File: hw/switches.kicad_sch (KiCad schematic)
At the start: 46 parts, among them SW1 SW_Push, SW10 SW_Push, SW11 SW_Push, SW12 SW_Push, SW13 SW_Push, SW14 SW_Push, SW15 SW_Push, SW16 SW_Push, SW17 SW_Push, SW18 SW_Push, SW19 SW_Push, SW2 SW_Push, SW20 SW_Push, SW21 SW_Push, SW3 SW_Push, SW4 SW_Push, SW5 SW_Push, SW6 SW_Push, SW7 SW_Push, SW8 SW_Push, SW9 SW_Push

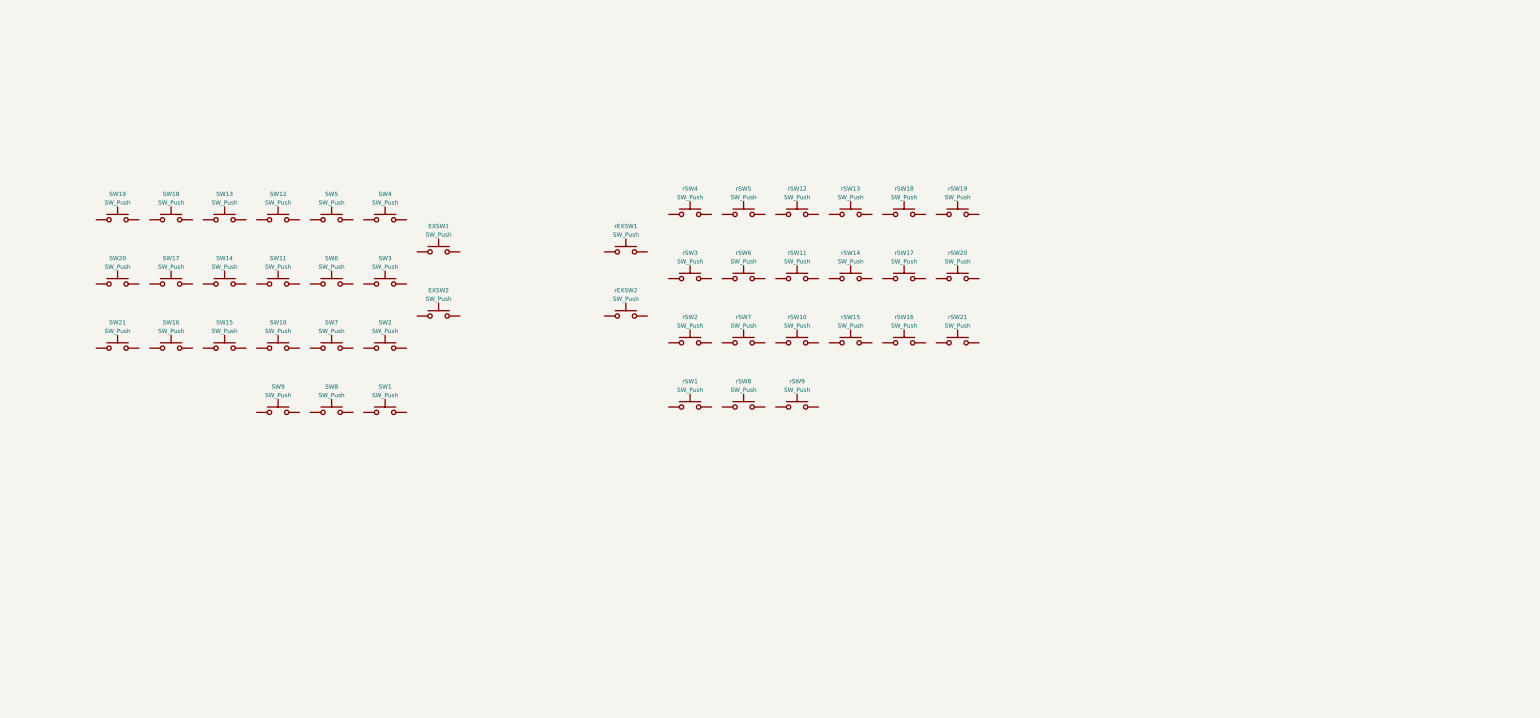
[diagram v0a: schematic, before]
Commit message: Power schematic with npm1100 setup
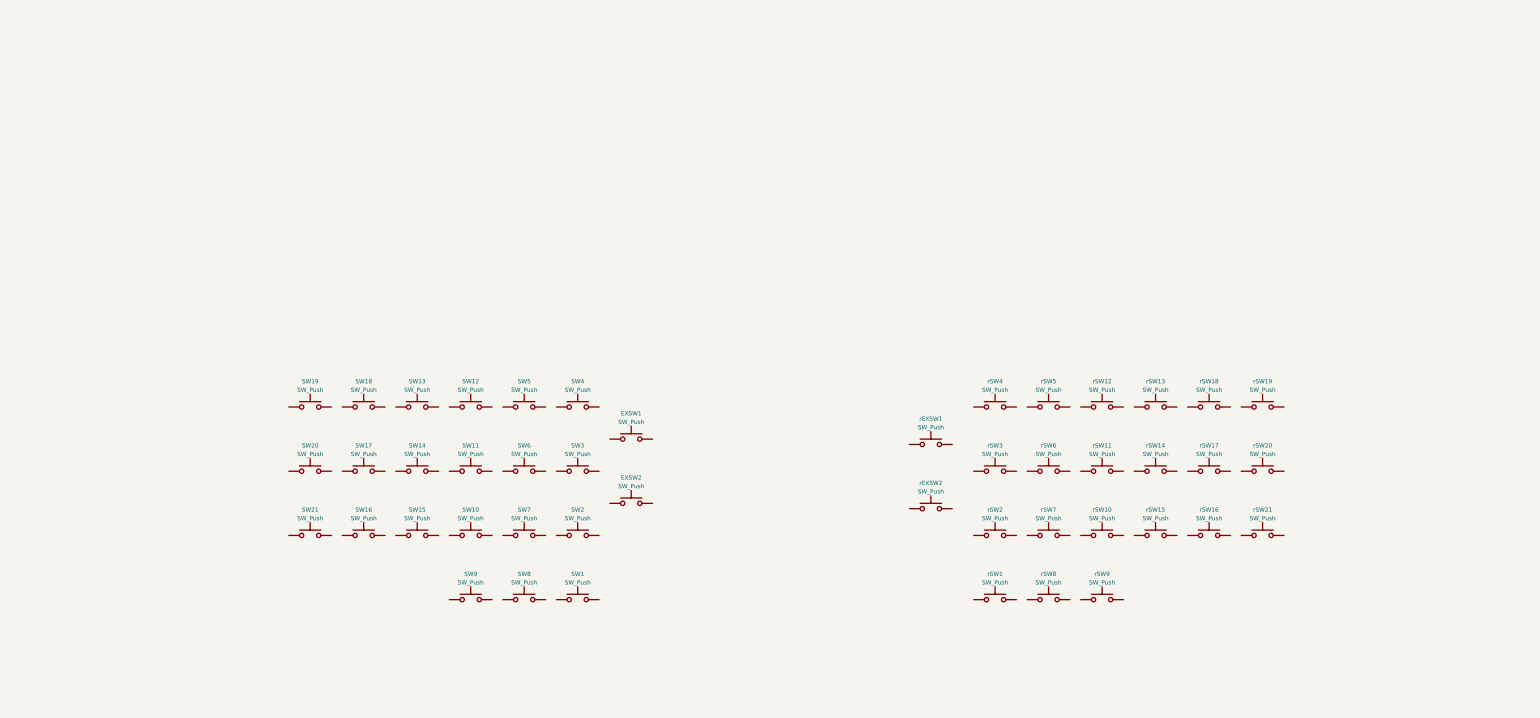
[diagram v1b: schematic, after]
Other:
- moved on the sheet: EXSW1, EXSW2, SW1, SW10, SW11, SW12, SW13, SW14, SW15, SW16, SW17, SW18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

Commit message: Switch matrix and sheet pins
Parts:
- added D1, D10, D11, D12, D13, D14, D15, D16, D17, D18, D19, D2, D20, D21, D22, D23, D3, D4, D5, D6, D7, D8, D9, rD1, rD10, rD11, rD12, rD13, rD14, rD15, rD16, rD17, rD18, rD19, rD2, rD20, rD21, rD22, rD23, rD3, rD4, rD5, rD6, rD7, rD8, rD9: D, symbol Alidade:D
- renumbered EXSW1 to SW22, EXSW2 to SW23, rEXSW1 to rSW22, rEXSW2 to rSW23
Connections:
- net at rSW6.1: now also rD6.2 (A)
- net rCOL2: now reaches rSW6.2
- net rCOL2: now also rSW5.2, rSW7.2, rSW8.2
- net at rSW4.1: now also rD4.2 (A)
- net rCOL1: now reaches rSW4.2
- net rCOL1: now also rSW1.2, rSW2.2, rSW3.2
- net at SW5.1: now also D5.2 (A)
- net COL2: now reaches SW5.2
- net COL2: now also SW6.2, SW7.2, SW8.2
- net at SW4.1: now also D4.2 (A)
- net COL1: now reaches SW4.2
- net COL1: now also SW1.2, SW2.2, SW3.2
- net at SW12.1: now also D12.2 (A)
- net COL3: now reaches SW12.2
- net COL3: now also SW10.2, SW11.2, SW9.2
- net at SW7.1: now also D7.2 (A)
- net at rSW5.1: now also rD5.2 (A)
- net at rSW16.1: now also rD16.2 (A)
- net rCOL5: now reaches rSW16.2
- net rCOL5: now also rSW17.2, rSW18.2
- net at SW21.1: now also D21.2 (A)
- net COL6: now reaches SW21.2
- net COL6: now also SW19.2, SW20.2
- net at rSW15.1: now also rD15.2 (A)
- net rCOL4: now reaches rSW15.2
- net rCOL4: now also rSW13.2, rSW14.2
- net at SW19.1: now also D19.2 (A)
- net at rSW1.1: now also rD1.2 (A)
- net at SW6.1: now also D6.2 (A)
- net at SW1.1: now also D1.2 (A)
- net at SW14.1: now also D14.2 (A)
- net COL4: now reaches SW14.2
- net COL4: now also SW13.2, SW15.2
- net at SW17.1: now also D17.2 (A)
- net COL5: now reaches SW17.2
- net COL5: now also SW16.2, SW18.2
- net at rSW17.1: now also rD17.2 (A)
- net at rSW21.1: now also rD21.2 (A)
- net rCOL6: now reaches rSW21.2
- net rCOL6: now also rSW19.2, rSW20.2
- net at SW16.1: now also D16.2 (A)
- net at SW15.1: now also D15.2 (A)
- net at SW18.1: now also D18.2 (A)
- net at rSW9.1: now also rD9.2 (A)
- net rCOL3: now reaches rSW9.2
- net rCOL3: now also rSW10.2, rSW11.2, rSW12.2
- net at SW23.1: now also D23.2 (A)
- net COL0: now reaches SW23.2
- net COL0: now also SW22.2
- net at rSW19.1: now also rD19.2 (A)
- net at rSW2.1: now also rD2.2 (A)
- net at rSW13.1: now also rD13.2 (A)
- net rCOL0: now reaches rSW23.1
- net rCOL0: now also rSW22.1
- net at rSW23.2: now also rD23.2 (A)
- net at rSW7.1: now also rD7.2 (A)
- net at SW2.1: now also D2.2 (A)
- net at rSW14.1: now also rD14.2 (A)
- net at rSW3.1: now also rD3.2 (A)
- net at SW11.1: now also D11.2 (A)
- net at rSW20.1: now also rD20.2 (A)
- net at SW20.1: now also D20.2 (A)
- net at rSW11.1: now also rD11.2 (A)
- net at SW22.1: now also D22.2 (A)
- net at SW13.1: now also D13.2 (A)
- net at rSW18.1: now also rD18.2 (A)
- net at rSW8.1: now also rD8.2 (A)
- net at SW8.1: now also D8.2 (A)
- net at rSW10.1: now also rD10.2 (A)
- net at rSW12.1: now also rD12.2 (A)
- net at SW9.1: now also D9.2 (A)
- net at rSW22.2: now also rD22.2 (A)
- net at SW3.1: now also D3.2 (A)
- net at SW10.1: now also D10.2 (A)
- new net ROW0: D1.1 (K), D8.1 (K), D9.1 (K)
- new net ROW1: D10.1 (K), D15.1 (K), D16.1 (K), D2.1 (K), D21.1 (K), D23.1 (K), D7.1 (K)
- new net ROW2: D11.1 (K), D14.1 (K), D17.1 (K), D20.1 (K), D22.1 (K), D3.1 (K), D6.1 (K)
- new net ROW3: D12.1 (K), D13.1 (K), D18.1 (K), D19.1 (K), D4.1 (K), D5.1 (K)
- new net rROW0: rD1.1 (K), rD8.1 (K), rD9.1 (K)
- new net rROW1: rD10.1 (K), rD15.1 (K), rD16.1 (K), rD2.1 (K), rD21.1 (K), rD23.1 (K), rD7.1 (K)
- new net rROW2: rD11.1 (K), rD14.1 (K), rD17.1 (K), rD20.1 (K), rD22.1 (K), rD3.1 (K), rD6.1 (K)
- new net rROW3: rD12.1 (K), rD13.1 (K), rD18.1 (K), rD19.1 (K), rD4.1 (K), rD5.1 (K)
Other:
- moved on the sheet: rSW22, rSW23

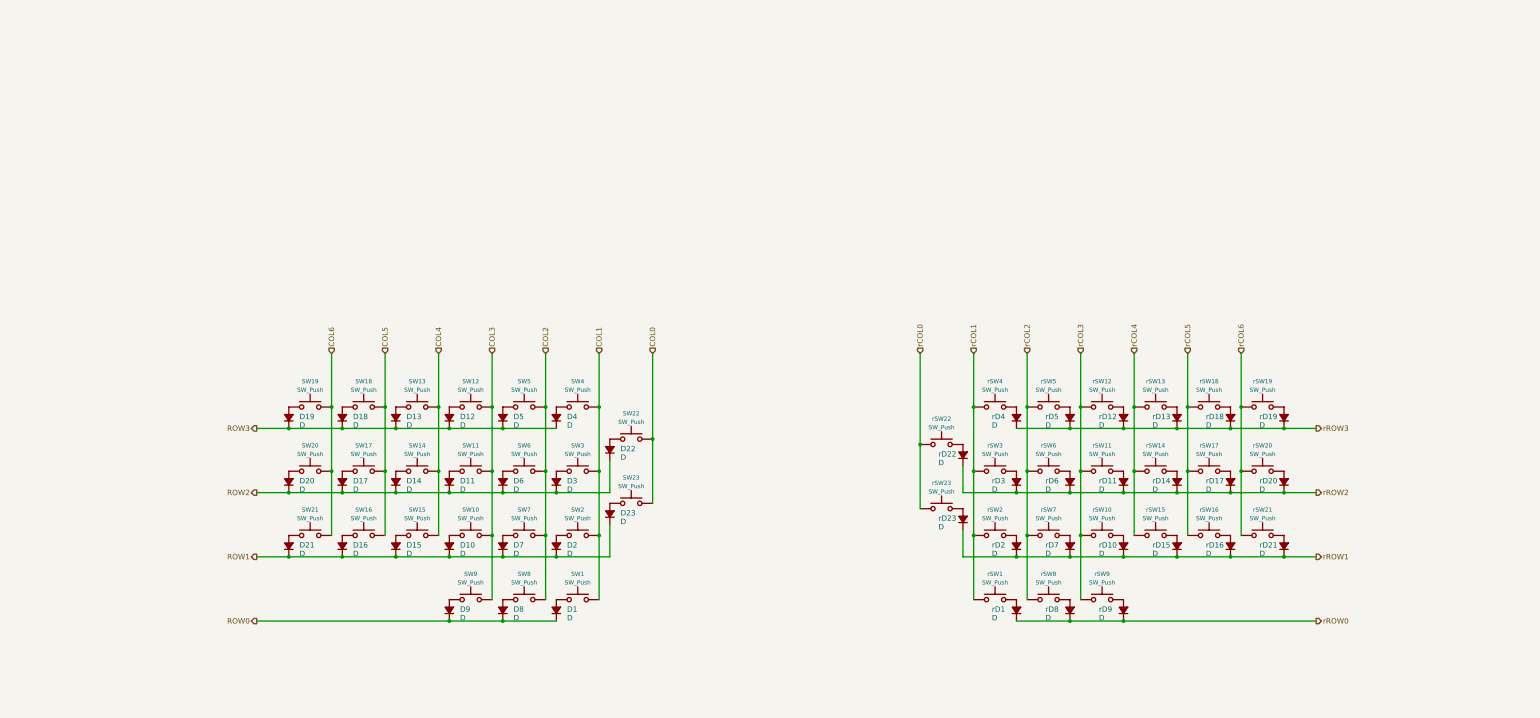
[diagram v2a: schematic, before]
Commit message: Place decoder and update switches
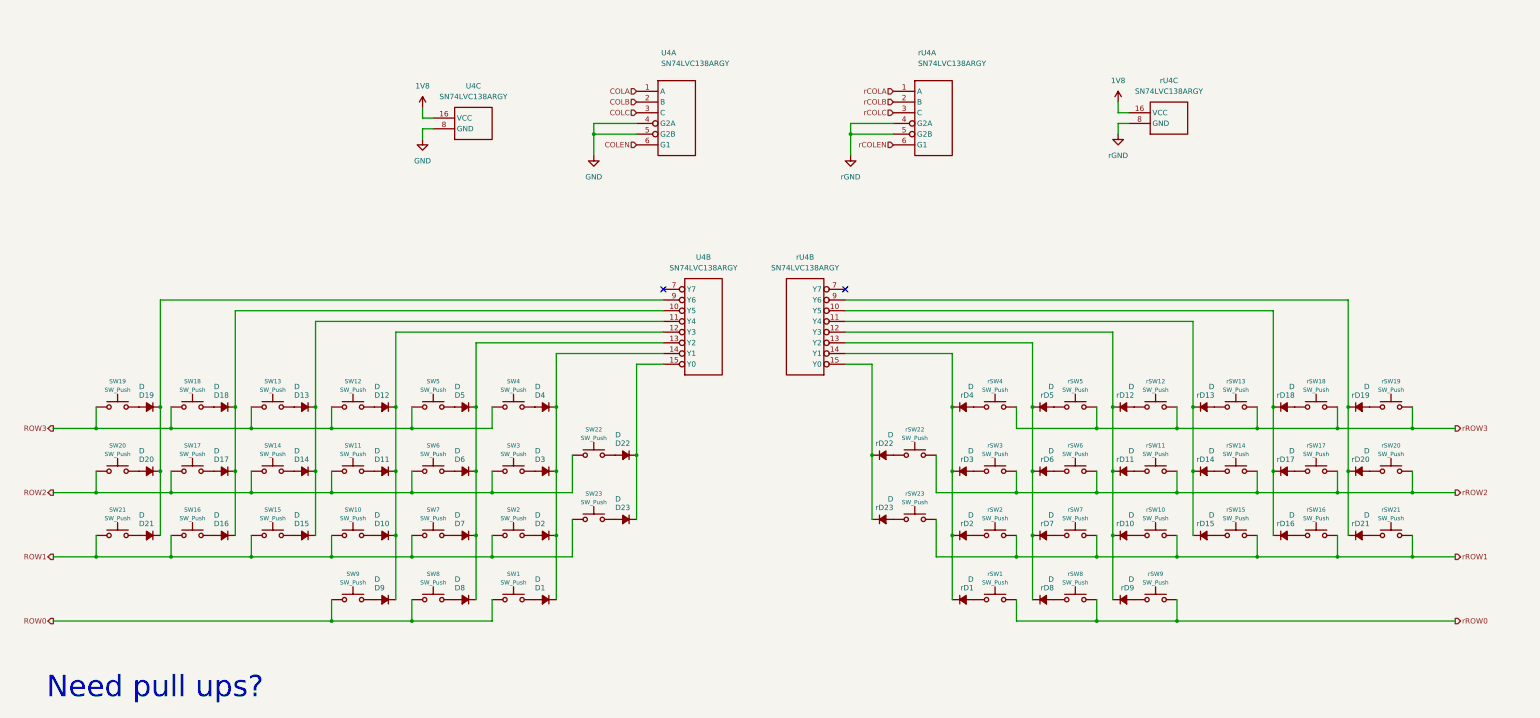
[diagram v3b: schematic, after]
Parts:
- added U4, rU4: SN74LVC138ARGY, symbol Alidade:SN74LVC138ARGY
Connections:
- net ROW0: now also SW1.1, SW8.1, SW9.1; no longer D1.1 (K), D8.1 (K), D9.1 (K)
- net ROW1: now also SW10.1, SW15.1, SW16.1, SW2.1, SW21.1, SW23.2, SW7.1; no longer D10.1 (K), D15.1 (K), D16.1 (K), D2.1 (K), D21.1 (K), D23.1 (K), D7.1 (K)
- net ROW2: now also SW11.1, SW14.1, SW17.1, SW20.1, SW22.2, SW3.1, SW6.1; no longer D11.1 (K), D14.1 (K), D17.1 (K), D20.1 (K), D22.1 (K), D3.1 (K), D6.1 (K)
- net ROW3: now also SW12.1, SW13.1, SW18.1, SW19.1, SW4.1, SW5.1; no longer D12.1 (K), D13.1 (K), D18.1 (K), D19.1 (K), D4.1 (K), D5.1 (K)
- net rROW0: now also rSW1.1, rSW8.1, rSW9.1; no longer rD1.1 (K), rD8.1 (K), rD9.1 (K)
- net rROW1: now also rSW10.1, rSW15.1, rSW16.1, rSW2.1, rSW21.1, rSW23.2, rSW7.1; no longer rD10.1 (K), rD15.1 (K), rD16.1 (K), rD2.1 (K), rD21.1 (K), rD23.1 (K), rD7.1 (K)
- net rROW2: now also rSW11.1, rSW14.1, rSW17.1, rSW20.1, rSW22.2, rSW3.1, rSW6.1; no longer rD11.1 (K), rD14.1 (K), rD17.1 (K), rD20.1 (K), rD22.1 (K), rD3.1 (K), rD6.1 (K)
- net rROW3: now also rSW12.1, rSW13.1, rSW18.1, rSW19.1, rSW4.1, rSW5.1; no longer rD12.1 (K), rD13.1 (K), rD18.1 (K), rD19.1 (K), rD4.1 (K), rD5.1 (K)
- net at rD6.2 (A): now also rSW6.2; no longer rSW6.1
- net at rD4.2 (A): now also rSW4.2; no longer rSW4.1
- net at D5.2 (A): now also SW5.2; no longer SW5.1
- net at rD21.2 (A): now also rSW21.2; no longer rSW21.1
- net at D4.2 (A): now also SW4.2; no longer SW4.1
- net at rD16.2 (A): now also rSW16.2; no longer rSW16.1
- net at D12.2 (A): now also SW12.2; no longer SW12.1
- net at D7.2 (A): now also SW7.2; no longer SW7.1
- net at D11.2 (A): now also SW11.2; no longer SW11.1
- net at rD5.2 (A): now also rSW5.2; no longer rSW5.1
- net at D8.2 (A): now also SW8.2; no longer SW8.1
- net at D21.2 (A): now also SW21.2; no longer SW21.1
- net at rD15.2 (A): now also rSW15.2; no longer rSW15.1
- net at D6.2 (A): now also SW6.2; no longer SW6.1
- net at D19.2 (A): now also SW19.2; no longer SW19.1
- net at rD1.2 (A): now also rSW1.2; no longer rSW1.1
- net at D16.2 (A): now also SW16.2; no longer SW16.1
- net at D20.2 (A): now also SW20.2; no longer SW20.1
- net at D15.2 (A): now also SW15.2; no longer SW15.1
- net at D1.2 (A): now also SW1.2; no longer SW1.1
- net at rD13.2 (A): now also rSW13.2; no longer rSW13.1
- net at D14.2 (A): now also SW14.2; no longer SW14.1
- net at D17.2 (A): now also SW17.2; no longer SW17.1
- net at rD17.2 (A): now also rSW17.2; no longer rSW17.1
- net at rD10.2 (A): now also rSW10.2; no longer rSW10.1
- net at rD14.2 (A): now also rSW14.2; no longer rSW14.1
- net at D18.2 (A): now also SW18.2; no longer SW18.1
- net at rD9.2 (A): now also rSW9.2; no longer rSW9.1
- net at D9.2 (A): now also SW9.2; no longer SW9.1
- net at rD19.2 (A): now also rSW19.2; no longer rSW19.1
- net at rD2.2 (A): now also rSW2.2; no longer rSW2.1
- net at rD23.2 (A): now also rSW23.1; no longer rSW23.2
- net at rD7.2 (A): now also rSW7.2; no longer rSW7.1
- net at D2.2 (A): now also SW2.2; no longer SW2.1
- net at D3.2 (A): now also SW3.2; no longer SW3.1
- net at rD12.2 (A): now also rSW12.2; no longer rSW12.1
- net at D13.2 (A): now also SW13.2; no longer SW13.1
- net at rD22.2 (A): now also rSW22.1; no longer rSW22.2
- net at rD3.2 (A): now also rSW3.2; no longer rSW3.1
- net at rD20.2 (A): now also rSW20.2; no longer rSW20.1
- net at rD11.2 (A): now also rSW11.2; no longer rSW11.1
- net at rD18.2 (A): now also rSW18.2; no longer rSW18.1
- net at rD8.2 (A): now also rSW8.2; no longer rSW8.1
- net at D10.2 (A): now also SW10.2; no longer SW10.1
- removed net COL0: SW22.2, SW23.2
- removed net COL1: SW1.2, SW2.2, SW3.2, SW4.2
- removed net COL2: SW5.2, SW6.2, SW7.2, SW8.2
- removed net COL3: SW10.2, SW11.2, SW12.2, SW9.2
- removed net COL4: SW13.2, SW14.2, SW15.2
- removed net COL5: SW16.2, SW17.2, SW18.2
- removed net COL6: SW19.2, SW20.2, SW21.2
- removed net rCOL0: rSW22.1, rSW23.1
- removed net rCOL1: rSW1.2, rSW2.2, rSW3.2, rSW4.2
- removed net rCOL2: rSW5.2, rSW6.2, rSW7.2, rSW8.2
- removed net rCOL3: rSW10.2, rSW11.2, rSW12.2, rSW9.2
- removed net rCOL4: rSW13.2, rSW14.2, rSW15.2
- removed net rCOL5: rSW16.2, rSW17.2, rSW18.2
- removed net rCOL6: rSW19.2, rSW20.2, rSW21.2
- new net: rD1.1 (K), rD2.1 (K), rD3.1 (K), rD4.1 (K), rU4.14 (Y1)
- new net: D5.1 (K), D6.1 (K), D7.1 (K), D8.1 (K), U4.13 (Y2)
- new net: D16.1 (K), D17.1 (K), D18.1 (K), U4.10 (Y5)
- new net: D13.1 (K), D14.1 (K), D15.1 (K), U4.11 (Y4)
- new net: D10.1 (K), D11.1 (K), D12.1 (K), D9.1 (K), U4.12 (Y3)
- new net: D1.1 (K), D2.1 (K), D3.1 (K), D4.1 (K), U4.14 (Y1)
- new net: D22.1 (K), D23.1 (K), U4.15 (Y0)
- new net: D19.1 (K), D20.1 (K), D21.1 (K), U4.9 (Y6)
- new net: rD16.1 (K), rD17.1 (K), rD18.1 (K), rU4.10 (Y5)
- new net: rD19.1 (K), rD20.1 (K), rD21.1 (K), rU4.9 (Y6)
- new net: rD5.1 (K), rD6.1 (K), rD7.1 (K), rD8.1 (K), rU4.13 (Y2)
- new net: rD13.1 (K), rD14.1 (K), rD15.1 (K), rU4.11 (Y4)
- new net: rD10.1 (K), rD11.1 (K), rD12.1 (K), rD9.1 (K), rU4.12 (Y3)
- new net: rD22.1 (K), rD23.1 (K), rU4.15 (Y0)
- new net 1V8: U4.16 (VCC), rU4.16 (VCC)
- new net COLA: U4.1 (A)
- new net COLB: U4.2 (B)
- new net COLC: U4.3 (C)
- new net COLEN: U4.6 (G1)
- new net GND: U4.4 (G2A), U4.5 (G2B), U4.8 (GND)
- new net rCOLA: rU4.1 (A)
- new net rCOLB: rU4.2 (B)
- new net rCOLC: rU4.3 (C)
- new net rCOLEN: rU4.6 (G1)
- new net rGND: rU4.4 (G2A), rU4.5 (G2B), rU4.8 (GND)
- no-connect marks 0 -> 2
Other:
- note added: "Need pull ups?"
- moved on the sheet: rSW10, rSW11, rSW12, rSW13, rSW14, rSW15, rSW16, rSW17, rSW18, rSW19, rSW20, rSW21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

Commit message: Place FPGA
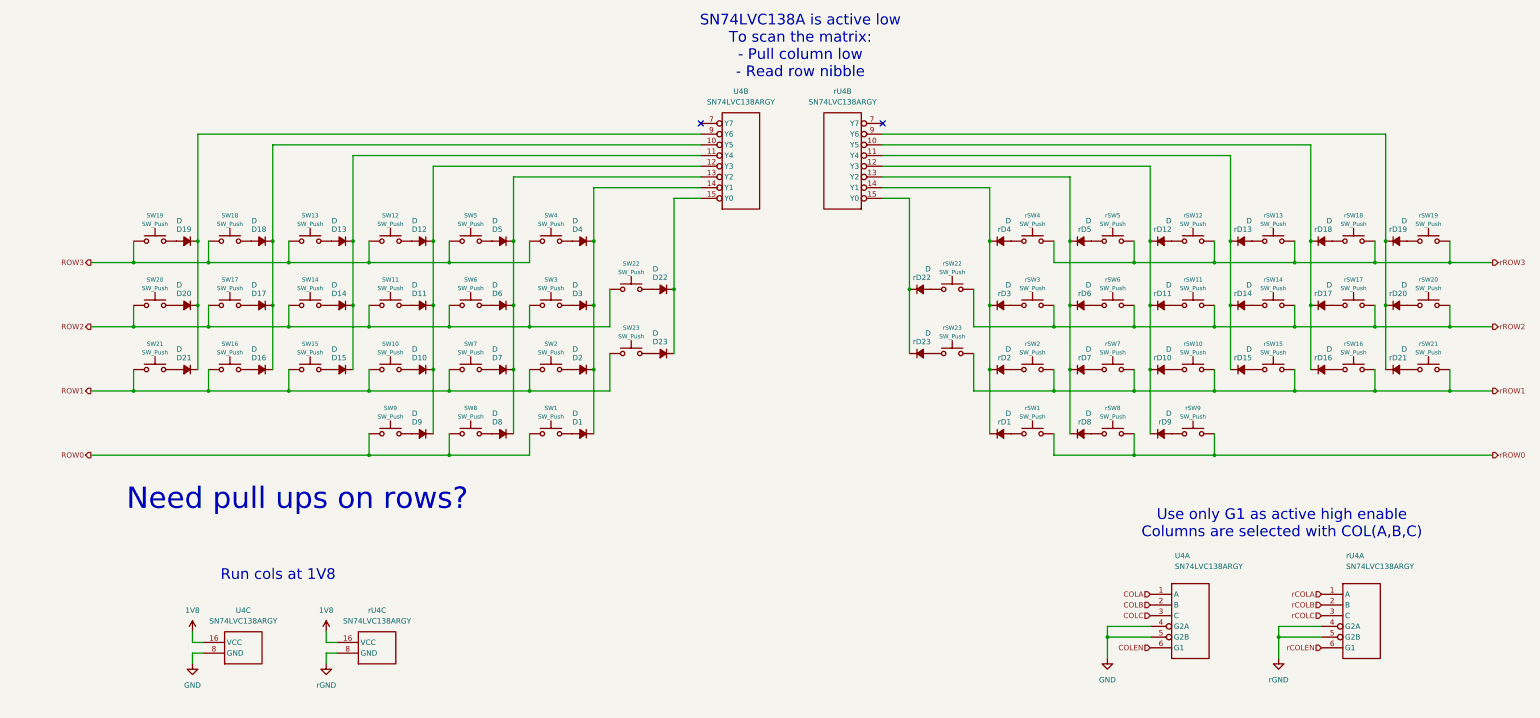
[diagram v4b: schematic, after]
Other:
- note added: "Need pull ups on rows?"
- note added: "Run cols at 1V8"
- note added: "SN74LVC138A is active low To scan the matrix: - Pull column low - Read row nibble"
- note added: "Use only G1 as active high enable Columns are selected with COL(A,B,C)"
- note removed: "Need pull ups?"
- moved on the sheet: D1, D10, D11, D12, D13, D14, D15, D16, D17, D18, D19, D2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
